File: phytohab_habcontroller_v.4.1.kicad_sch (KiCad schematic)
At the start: 0 parts

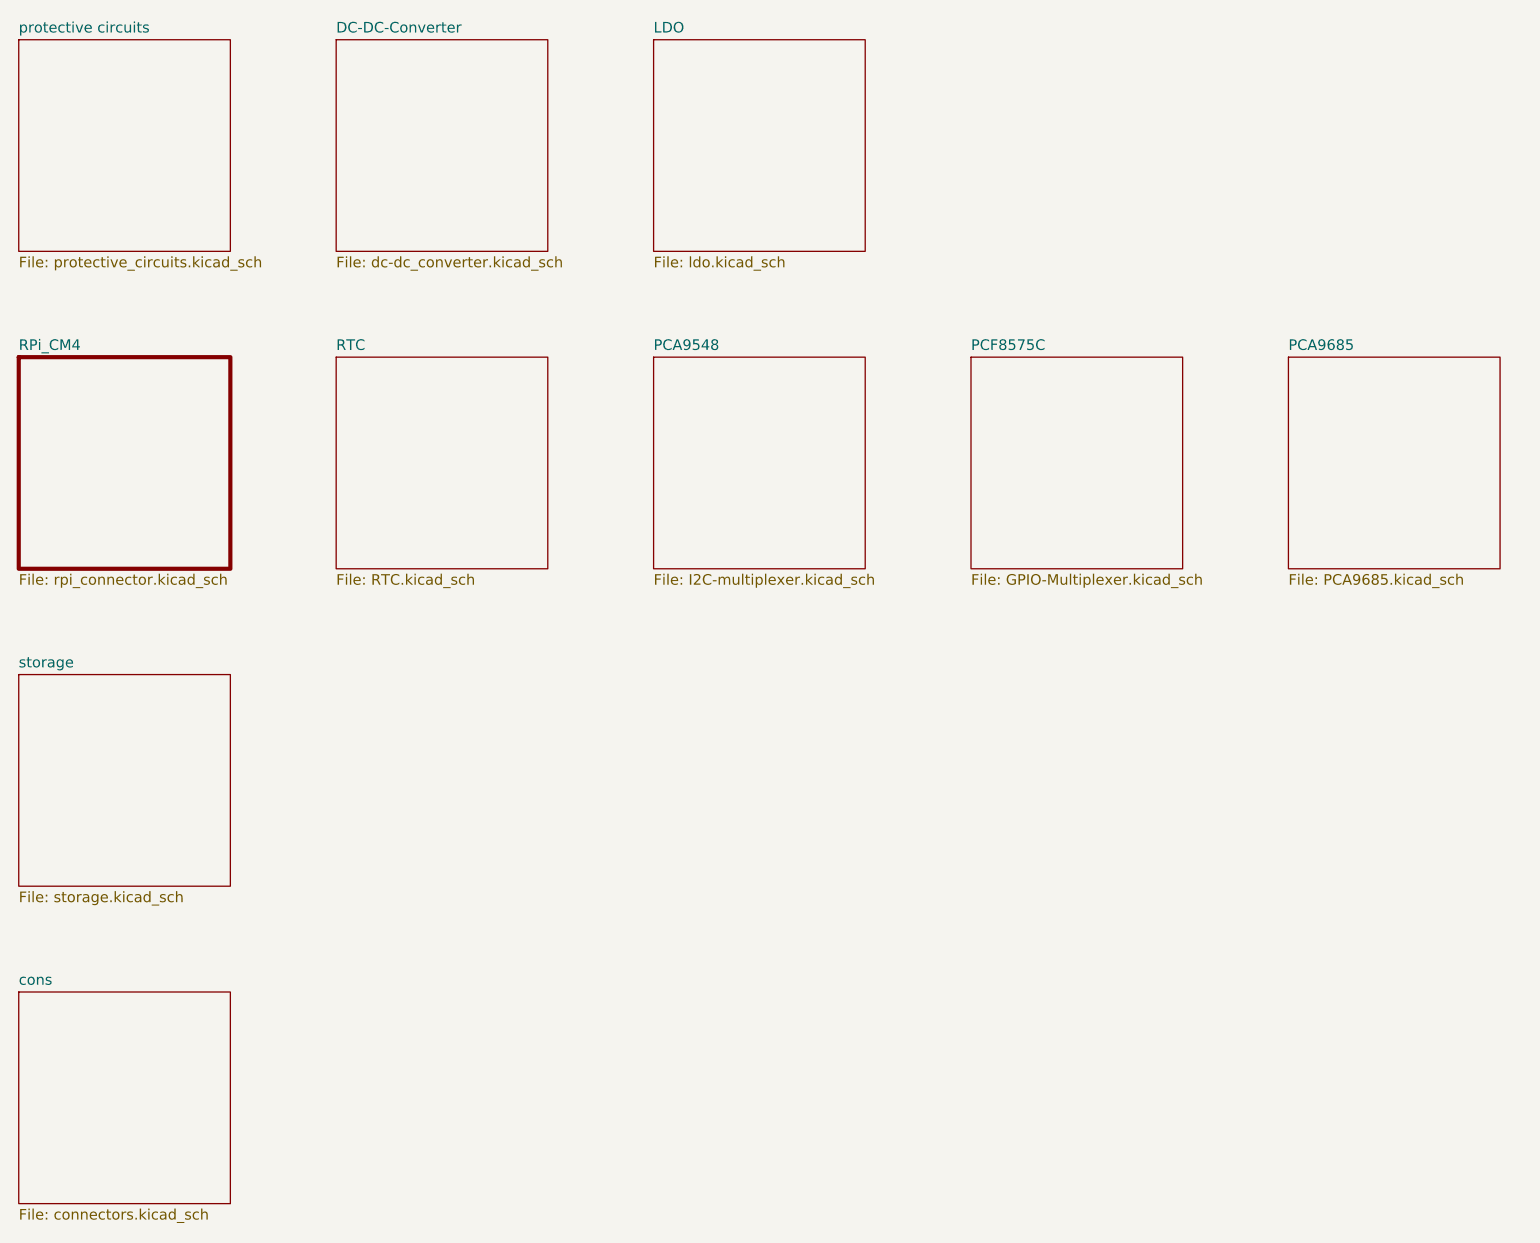
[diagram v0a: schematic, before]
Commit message: CM4>RP3/4
changed SBC to RP3/4
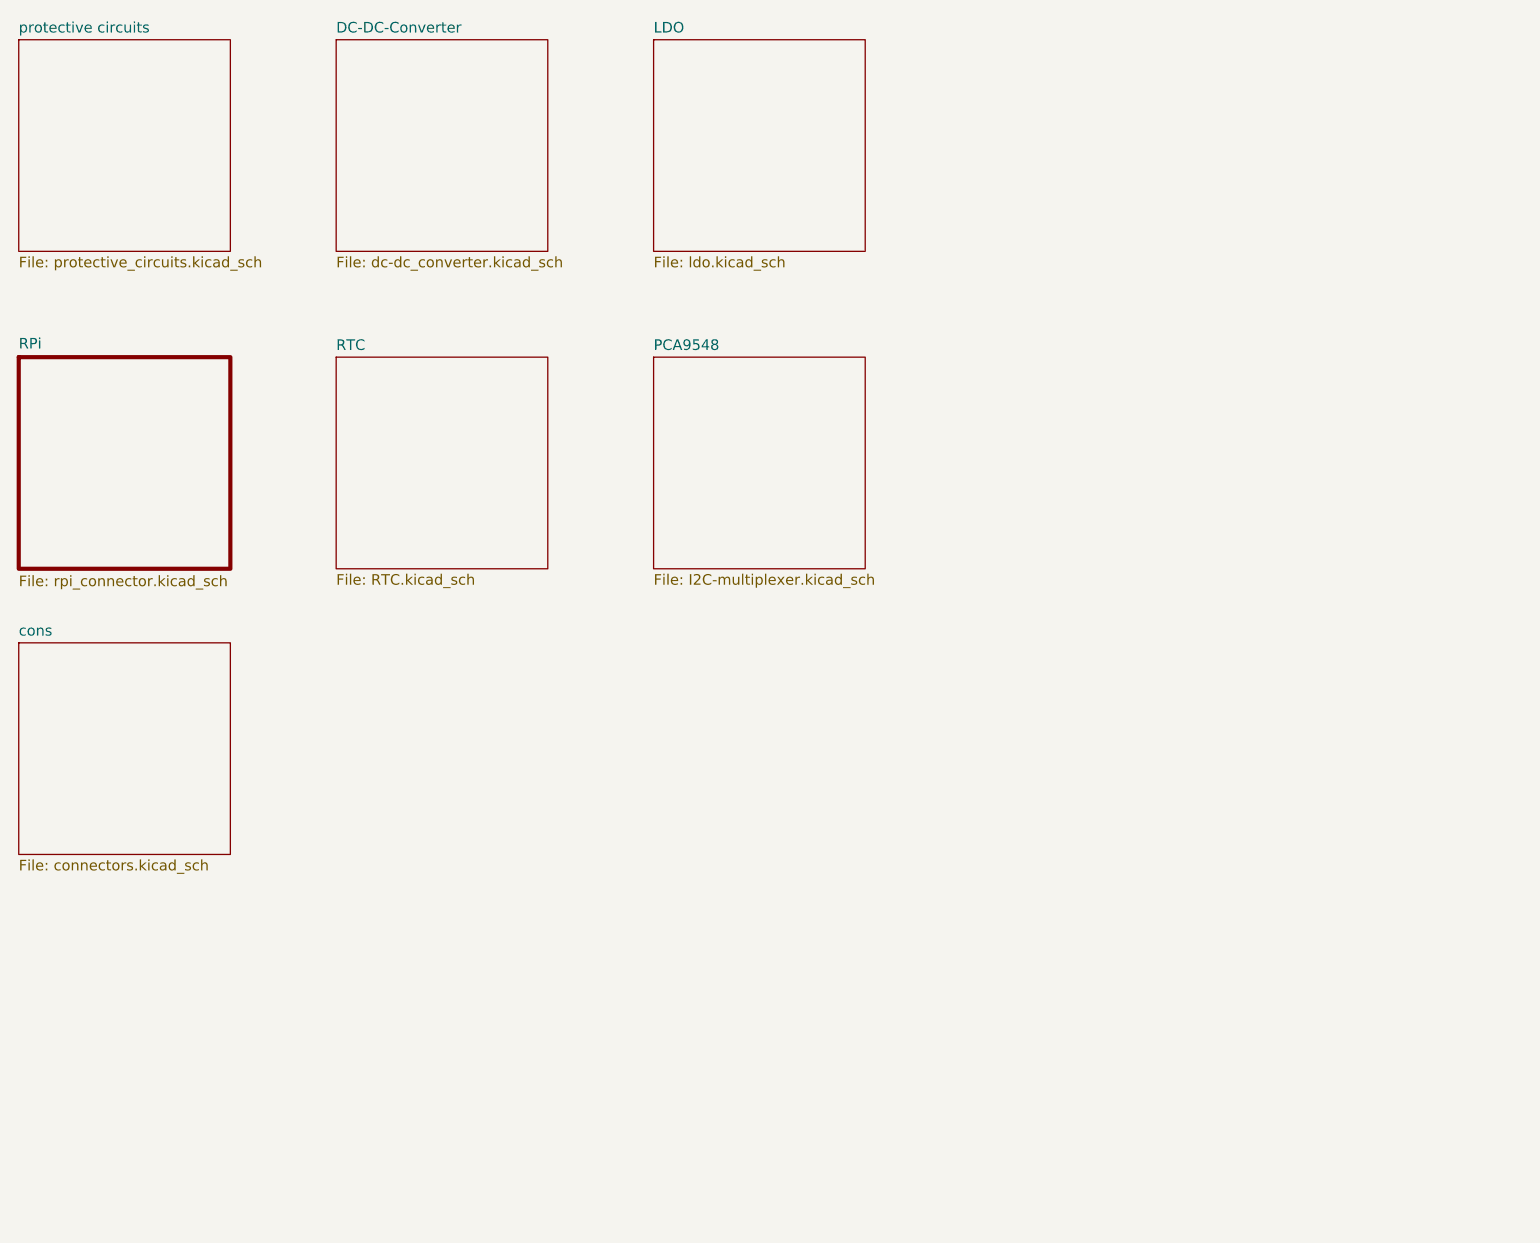
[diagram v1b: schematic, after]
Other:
- sheet RPi_CM4 renamed RPi
- removed sheet PCA9685
- removed sheet PCF8575C
- removed sheet storage
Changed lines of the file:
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@@
 	(paper "A4")
-	(sheet
-		(at 25.4 101.6)
-		(size 25.4 25.4)
-		(fields_autoplaced yes)
-		(stroke
-			(width 0.1524)
-			(type solid)
-		)
-		(fill
-			(color 0 0 0 0.0000)
-		)
-		(property "Sheetname" "storage"
-			(at 25.4 100.8884 0)
-			(effects
-				(font
-					(size 1.27 1.27)
-				)
-				(justify left bottom)
-			)
-		)
-		(property "Sheetfile" "storage.kicad_sch"
-			(at 25.4 127.5846 0)
-			(effects
-				(font
-					(size 1.27 1.27)
-				)
-				(justify left top)
-			)
-		)
-		(instances
-			(project "phytohab_habcontroller_v.4.1"
-				(path "/63d8ebc3-d81d-4869-925f-b28ad884a523"
-					(page "900")
-				)
-			)
-		)
-	)
-	(sheet
-		(at 139.7 63.5)
-		(size 25.4 25.4)
-		(fields_autoplaced yes)
-		(stroke
-			(width 0.1524)
-			(type solid)
-			(color 0 255 34 1)
-		)
-		(fill
-			(color 0 0 0 0.0000)
-		)
-		(property "Sheetname" "PCF8575C"
-			(at 139.7 62.7884 0)
-			(effects
-				(font
-					(size 1.27 1.27)
-				)
-				(justify left bottom)
-			)
-		)
-		(property "Sheetfile" "GPIO-Multiplexer.kicad_sch"
-			(at 139.7 89.4846 0)
-			(effects
-				(font
-					(size 1.27 1.27)
-				)
-				(justify left top)
-			)
-		)
-		(property "Feld2" ""
-			(at 139.7 63.5 0)
-			(effects
-				(font
-					(size 1.27 1.27)
-				)
-				(hide yes)
-			)
-		)
-		(instances
-			(project "phytohab_habcontroller_v.4.1"
-				(path "/63d8ebc3-d81d-4869-925f-b28ad884a523"
-					(page "700")
-				)
-			)
-		)
-	)
 	(sheet
 		(at 63.5 25.4)
@@
 	)
 	(sheet
-		(at 177.8 63.5)
-		(size 25.4 25.4)
-		(fields_autoplaced yes)
-		(stroke
-			(width 0.1524)
-			(type solid)
-			(color 7 255 10 1)
-		)
-		(fill
-			(color 0 0 0 0.0000)
-		)
-		(property "Sheetname" "PCA9685"
-			(at 177.8 62.7884 0)
-			(effects
-				(font
-					(size 1.27 1.27)
-				)
-				(justify left bottom)
-			)
-		)
-		(property "Sheetfile" "PCA9685.kicad_sch"
-			(at 177.8 89.4846 0)
-			(effects
-				(font
-					(size 1.27 1.27)
-				)
-				(justify left top)
-			)
-		)
-		(instances
-			(project "phytohab_habcontroller_v.4.1"
-				(path "/63d8ebc3-d81d-4869-925f-b28ad884a523"
-					(page "800")
-				)
-			)
-		)
-	)
-	(sheet
 		(at 25.4 63.5)
 		(size 25.4 25.4)
@@
 			(color 0 0 0 0.0000)
 		)
-		(property "Sheetname" "RPi_CM4"
-			(at 25.4 62.7884 0)
+		(property "Sheetname" "RPi"
+			(at 25.4 62.6146 0)
 			(effects
 				(font
@@
 		)
 		(property "Sheetfile" "rpi_connector.kicad_sch"
-			(at 25.4 89.4846 0)
+			(at 25.4 89.6584 0)
 			(effects
 				(font
@@
 	)
 	(sheet
-		(at 25.4 139.7)
+		(at 25.4 97.79)
 		(size 25.4 25.4)
 		(fields_autoplaced yes)
@@
 		)
 		(property "Sheetname" "cons"
-			(at 25.4 138.9884 0)
+			(at 25.4 97.0784 0)
 			(effects
 				(font
@@
 		)
 		(property "Sheetfile" "connectors.kicad_sch"
-			(at 25.4 165.6846 0)
+			(at 25.4 123.7746 0)
 			(effects
 				(font
